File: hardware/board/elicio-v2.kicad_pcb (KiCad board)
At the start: 2 copper layers, 32.7 x 55.2 mm, 66 parts, among them J2 SM02B-SRSS-TB, J3 HDR-3-RA, J4 TC2030-NL, P1 SIG1, P2 SIG2, P3 REF, P4 CHARGE_VBUS, P5 CHARGE_GND, Q1 AO3401A, Q2 2N7002, Q3 2N7002, Q4 2N7002, Q5 2N7002, SW1 4.5x4.5x1.6, U1 MDBT50Q-1MV2, U2 ADS1292IRSMT, U3 BQ25100YFPR, U4 TLV71330PDBVR

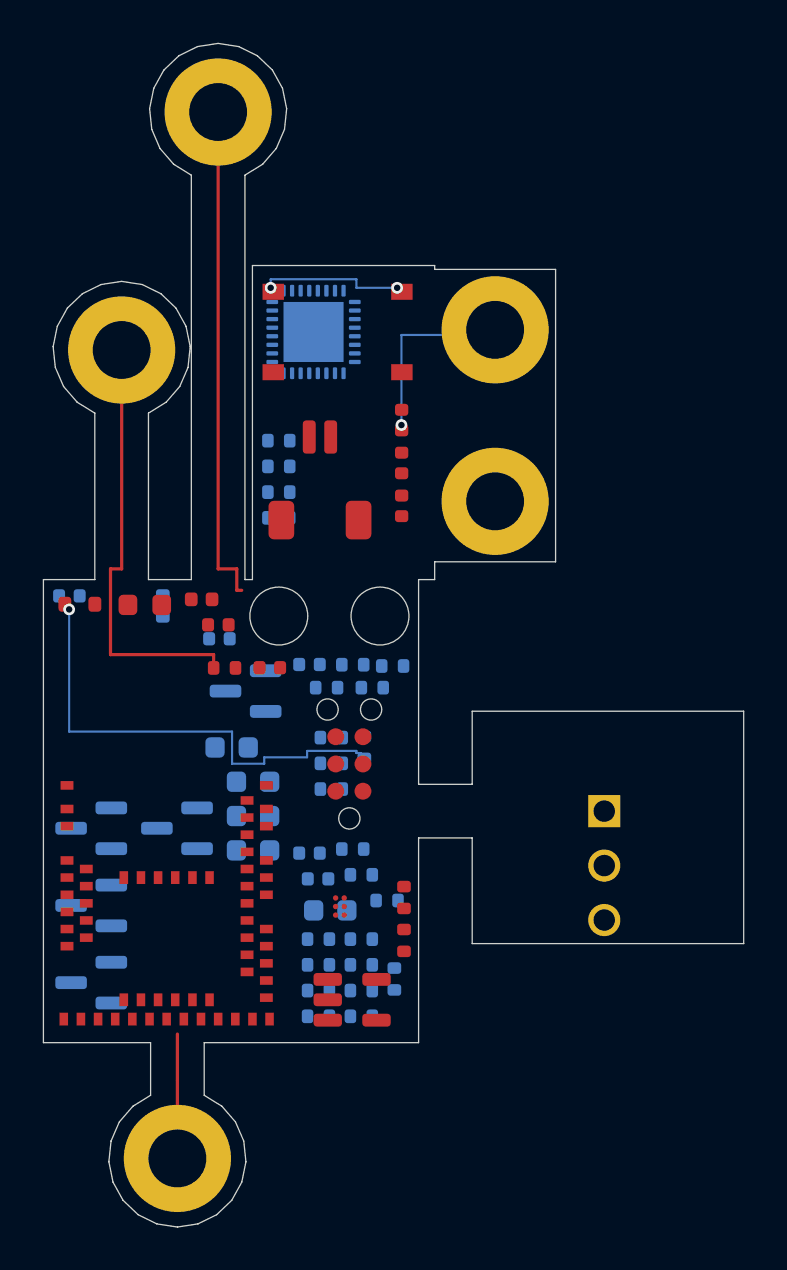
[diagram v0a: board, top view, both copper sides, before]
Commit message: board(v3): retain DRC-clean partial routing and export PI stiffener layer
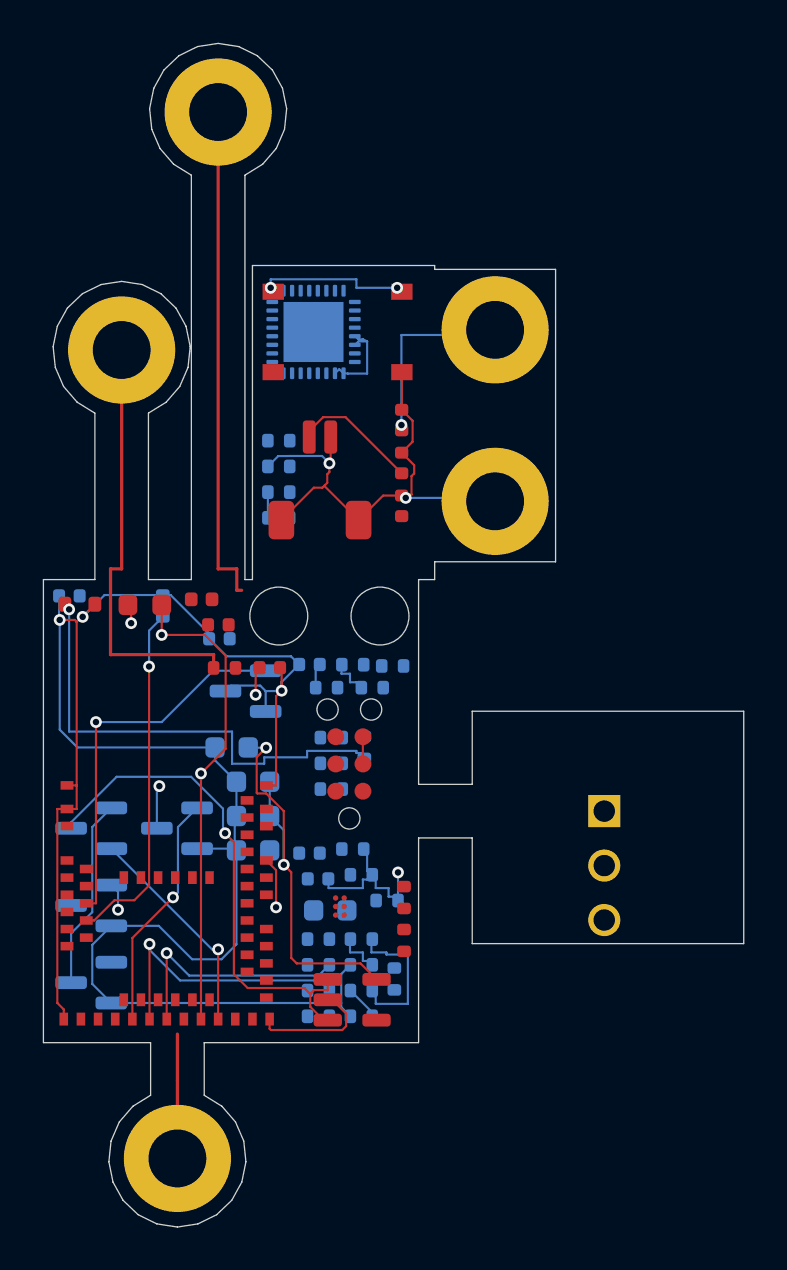
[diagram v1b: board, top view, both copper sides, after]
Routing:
- net GND: track 0.00 -> 128.7 mm, vias 0 -> 5
- net +3V0: track 0.00 -> 24.7 mm, vias 0 -> 2
- net VBAT: track 0.00 -> 23.9 mm, vias 0 -> 2
- net AFE_VIN: track 0.00 -> 23.8 mm, vias 0 -> 1
- net +VDD: track 0.00 -> 23.4 mm, vias 0 -> 2
- net BAT_MEAS_EN: track 0.00 -> 17.8 mm, vias 0 -> 1
- net VBAT_SENSE: track 0.00 -> 16.4 mm, vias 0 -> 1
- net AFE_MOSI: track 0.00 -> 13.0 mm, vias 0 -> 1
- net AFE_SCLK: track 0.00 -> 11.3 mm, vias 0 -> 1
- net LED_EN: track 0.00 -> 11.1 mm, vias 0 -> 1
- net AFE_GATE: track 0.00 -> 8.93 mm
- net VBUS: track 31.1 -> 38.0 mm
- net VBUS_DET: track 0.00 -> 4.00 mm, vias 0 -> 1
- net Q2_G: track 0.00 -> 3.40 mm, vias 0 -> 1
- net CHG_LED_K: track 0.00 -> 2.01 mm, vias 0 -> 1
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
